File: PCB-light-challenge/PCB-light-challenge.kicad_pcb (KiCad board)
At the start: 2 copper layers, 1 part

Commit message: Footprints toegevoegd van alles
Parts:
- removed U-PICO2: ~, custom_footprint_pico:Pico_light challenge
- added 3V3: Screw_Terminal_01x02, Connector_PinHeader_2.54mm:PinHeader_1x02_P2.54mm_Horizontal, F.Cu at (74.2, 33.9)
- added 5V1: Screw_Terminal_01x02, Connector_PinHeader_2.54mm:PinHeader_1x02_P2.54mm_Horizontal, F.Cu at (75.3, 44.1)
- added Batterij1: Screw_Terminal_01x02, Connector_PinHeader_2.54mm:PinHeader_1x02_P2.54mm_Horizontal, F.Cu at (76.2, 53.7)
- added C1: 100n, Capacitor_SMD:C_0603_1608Metric, F.Cu at (211.5, 144.0)
- added C2: 100n, Capacitor_SMD:C_0603_1608Metric, F.Cu at (189.5, 140.0)
- added J2: Screw_Terminal_01x20, Connector_PinHeader_2.54mm:PinHeader_1x35_P2.54mm_Horizontal, F.Cu at (54.4, 23.3)
- added PIR_sens1: ~, PIRsens:PIR-SENS, F.Cu at (202.0, 126.0)
- added PS2: TMPW_5-105, TMPW_5-105:CONV_TMPW_5-105, F.Cu at (254.7, 135.7)
- added R1: 330, Resistor_SMD:R_0603_1608Metric, F.Cu at (206.1, 146.6)
- added R2: 2K7, Resistor_SMD:R_0603_1608Metric, F.Cu at (206.1, 149.1)
- added Shock_sens1: ~, Shocksens:Schock-sens, F.Cu at (179.7, 139.7)
- added U-PICO1: ~, Pico footprint:PICO, F.Cu at (215.1, 105.9)
- added U1: ~, BMS:bms, F.Cu at (167.7, 77.5)
- added U2: AP9101CK, Package_TO_SOT_SMD:SOT-23-5, F.Cu at (216.0, 136.1)
- added U3: SP8K32FRATB, MOSFET footprint:SOIC127P600X175-8N, F.Cu at (225.2, 135.6)
- added U4: ~, LDO:LDO- TO220FP, F.Cu at (198.5, 138.5)
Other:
- board outline added: 80.1 x 79.1 mm

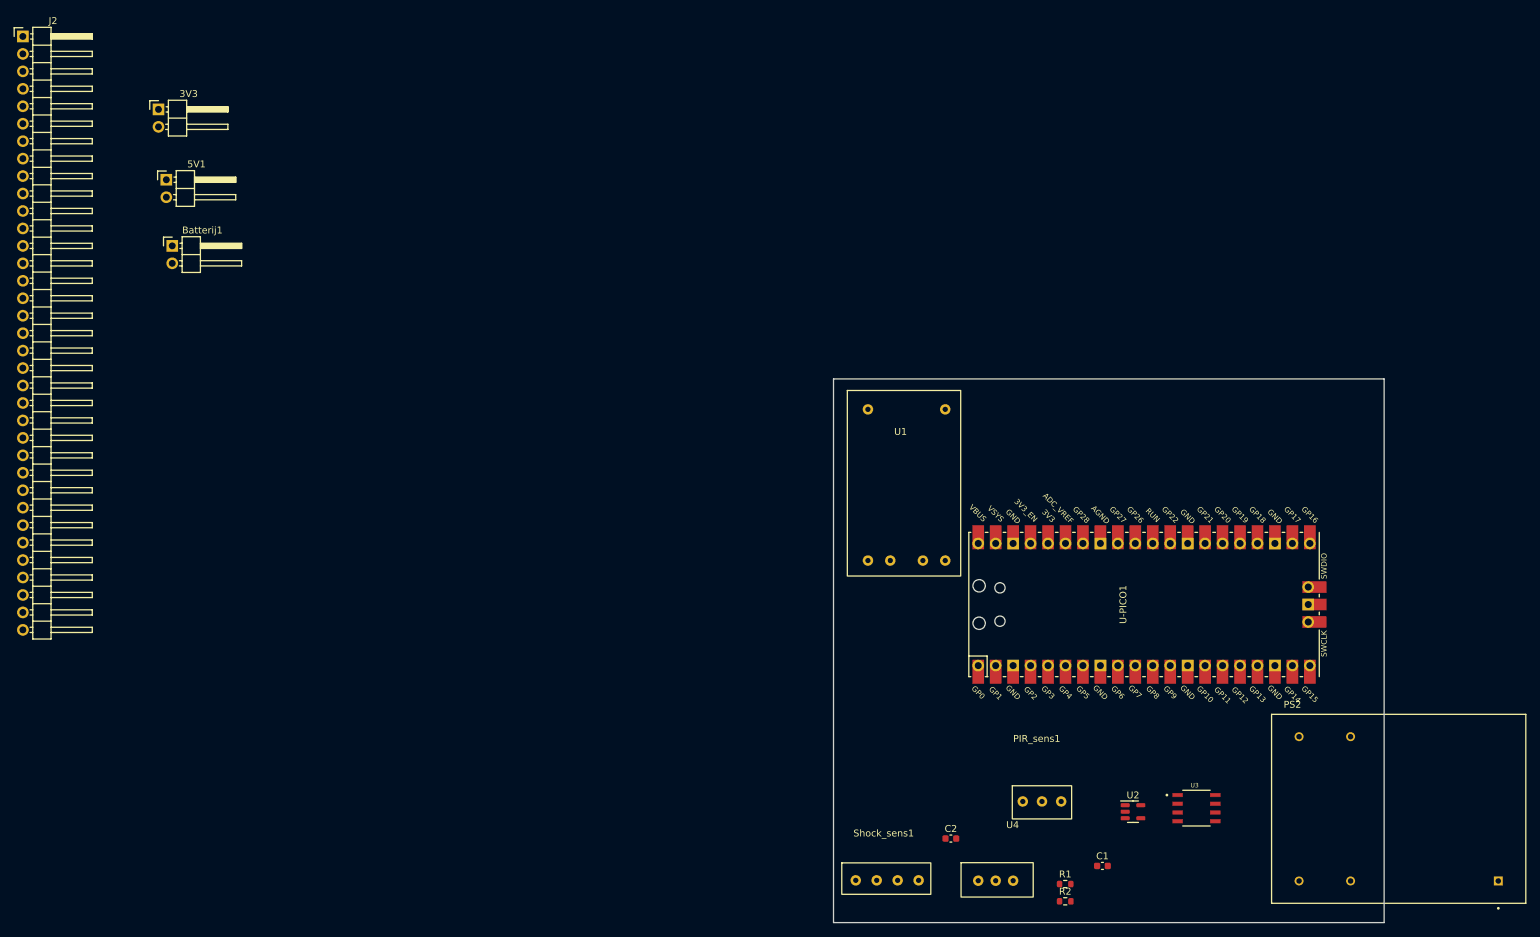
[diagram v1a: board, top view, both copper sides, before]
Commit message: Mainboard onderdelen gesorteerd
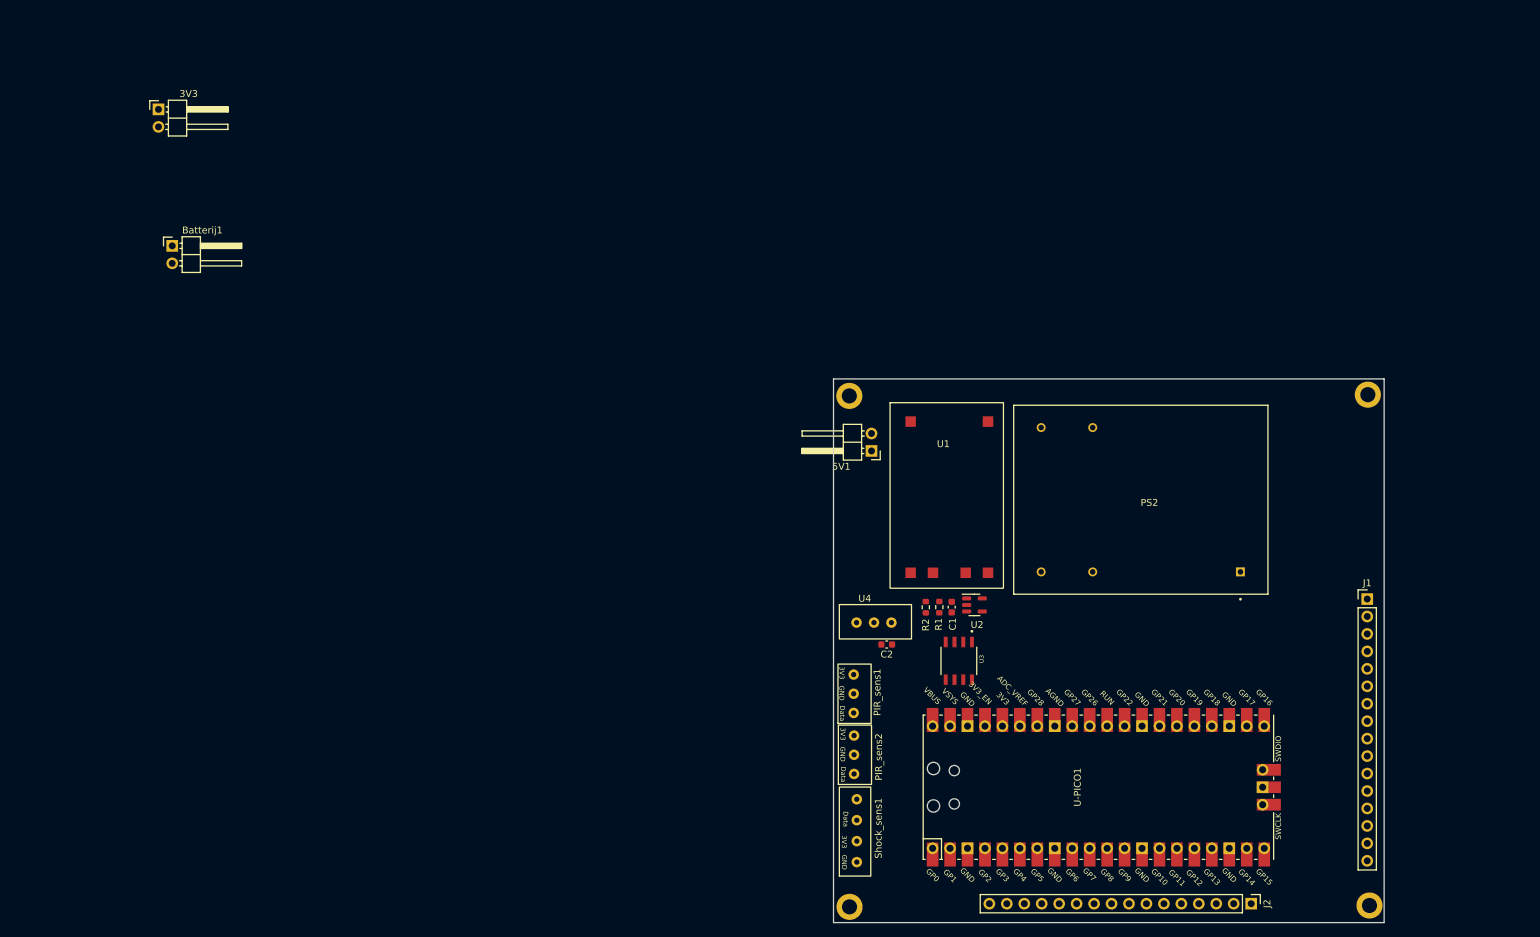
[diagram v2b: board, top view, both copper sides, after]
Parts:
- added H1: MountingHole_Pad, MountingHole:MountingHole_2.2mm_M2_DIN965_Pad, F.Cu at (174.7, 75.6)
- added H2: MountingHole_Pad, MountingHole:MountingHole_2.2mm_M2_DIN965_Pad, F.Cu at (250.4, 149.7)
- added H3: MountingHole_Pad, MountingHole:MountingHole_2.2mm_M2_DIN965_Pad, F.Cu at (250.2, 75.4)
- added H4: MountingHole_Pad, MountingHole:MountingHole_2.2mm_M2_DIN965_Pad, F.Cu at (174.7, 149.9)
- added J1: Conn_01x16_Socket, Connector_PinHeader_2.54mm:PinHeader_1x16_P2.54mm_Vertical, F.Cu at (250.1, 105.1)
- added PIR_sens2: ~, PIRsens:PIR-SENS, F.Cu at (166.8, 128.6)
- J2: value Screw_Terminal_01x20 -> Conn_01x16_Socket; footprint Connector_PinHeader_2.54mm:PinHeader_1x35_P2.54mm_Horizontal -> Connector_PinHeader_2.54mm:PinHeader_1x16_P2.54mm_Vertical
- moved J2 218.8 mm to (233.2, 149.5), turned to -90 degrees
- moved 5V1 110.0 mm to (177.9, 83.6), turned to 180 degrees
- moved PS2 58.6 mm to (217.1, 90.7)
- moved R2 47.4 mm to (185.8, 106.3), turned to -90 degrees
- moved R1 44.3 mm to (187.8, 106.3), turned to 90 degrees
- moved C1 43.6 mm to (189.6, 106.3), turned to -90 degrees
- moved U4 41.5 mm to (180.8, 100.9)
- moved U3 40.7 mm to (190.6, 114.1), turned to -90 degrees
- moved U2 37.9 mm to (192.9, 106.0)
- moved PIR_sens1 35.8 mm to (166.7, 119.7), turned to 90 degrees
- moved C2 29.7 mm to (180.1, 111.8), turned to 180 degrees
- moved U-PICO1 27.4 mm to (208.4, 132.5)
- moved Shock_sens1 10.3 mm to (169.4, 139.3), turned to 90 degrees
- moved U1 6.47 mm to (173.9, 79.3)
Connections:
- J2 pad 1: BAT- -> GP15
- J2 pad 10: GP28 -> GP6
- J2 pad 11: GP27 -> GP5
- J2 pad 12: GP26 -> GP4
- J2 pad 13: GP22 -> GP3
- J2 pad 14: GP21 -> GP2
- J2 pad 15: GP20 -> GP1
- J2 pad 16: GP19 -> GP0
- J2 pad 2: 3V3 -> GP14
- J2 pad 3: VBUS -> GP13
- J2 pad 4: RUN -> GP12
- J2 pad 5: ADC VREF -> GP11
- J2 pad 6: 3V3 OUT -> GP10
- J2 pad 7: 3V3 EN -> GP9
- J2 pad 8: SWDIO -> GP8
- J2 pad 9: SWCLK -> GP7
- U-PICO1 pad 1: (no net) -> GP0
- U-PICO1 pad 10: (no net) -> GP7
- U-PICO1 pad 11: (no net) -> GP8
- U-PICO1 pad 12: (no net) -> GP9
- U-PICO1 pad 13: (no net) -> BAT-
- U-PICO1 pad 14: (no net) -> GP10
- U-PICO1 pad 15: (no net) -> GP11
- U-PICO1 pad 16: (no net) -> GP12
- U-PICO1 pad 17: (no net) -> GP13
- U-PICO1 pad 18: (no net) -> BAT-
- U-PICO1 pad 19: (no net) -> GP14
- U-PICO1 pad 2: (no net) -> GP1
- U-PICO1 pad 20: (no net) -> GP15
- U-PICO1 pad 21: (no net) -> GP16
- U-PICO1 pad 22: (no net) -> GP17
- U-PICO1 pad 23: (no net) -> BAT-
- U-PICO1 pad 24: (no net) -> GP18
- U-PICO1 pad 25: (no net) -> GP19
- U-PICO1 pad 26: (no net) -> GP20
- U-PICO1 pad 27: (no net) -> GP21
- U-PICO1 pad 28: (no net) -> BAT-
- U-PICO1 pad 29: (no net) -> GP22
- U-PICO1 pad 3: (no net) -> BAT-
- U-PICO1 pad 30: (no net) -> RUN
- U-PICO1 pad 31: (no net) -> GP26
- U-PICO1 pad 32: (no net) -> GP27
- U-PICO1 pad 33: (no net) -> BAT-
- U-PICO1 pad 34: (no net) -> GP28
- U-PICO1 pad 35: (no net) -> ADC VREF
- U-PICO1 pad 36: (no net) -> 3V3 OUT
- U-PICO1 pad 37: (no net) -> 3V3 EN
- U-PICO1 pad 38: (no net) -> BAT-
- U-PICO1 pad 39: (no net) -> 3V3
- U-PICO1 pad 4: (no net) -> GP2
- U-PICO1 pad 40: (no net) -> VBUS
- U-PICO1 pad 5: (no net) -> GP3
- U-PICO1 pad 6: (no net) -> GP4
- U-PICO1 pad 7: (no net) -> GP5
- U-PICO1 pad 8: (no net) -> BAT-
- U-PICO1 pad 9: (no net) -> GP6
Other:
- board text added: "3V3"
- board text added: "Data"
- board text added: "GND"

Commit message: main board aangepast en ground toegevoegd
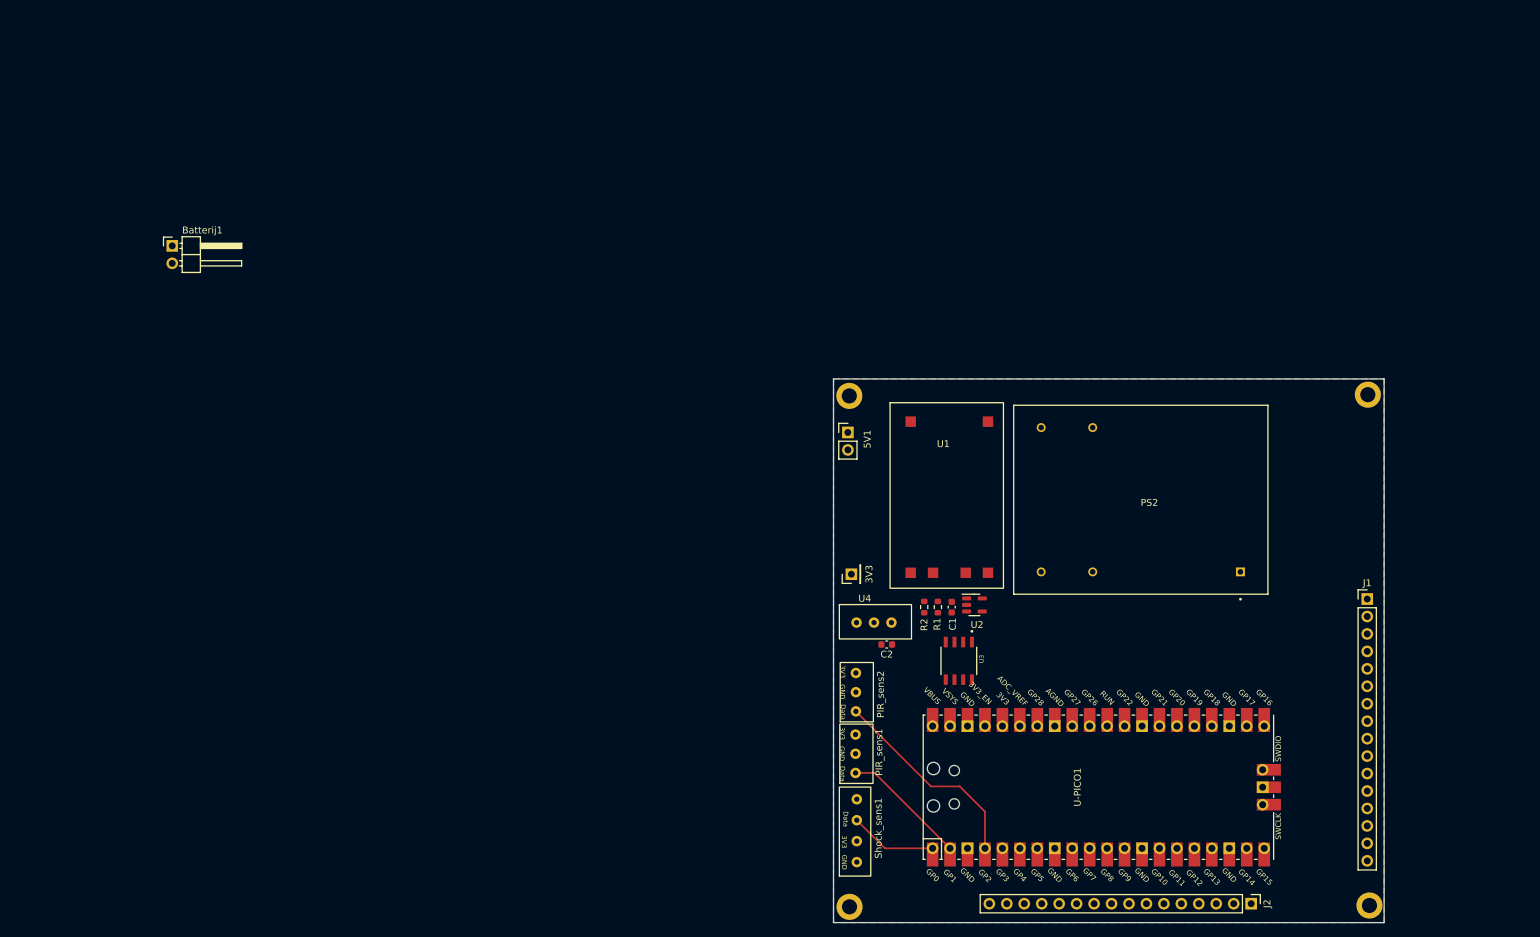
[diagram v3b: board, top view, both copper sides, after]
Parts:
- 3V3: value Screw_Terminal_01x02 -> Conn_01x01_Socket; footprint Connector_PinHeader_2.54mm:PinHeader_1x02_P2.54mm_Horizontal -> Connector_PinHeader_2.54mm:PinHeader_1x01_P2.54mm_Vertical
- 5V1: value Screw_Terminal_01x02 -> Conn_01x02_Socket; footprint Connector_PinHeader_2.54mm:PinHeader_1x02_P2.54mm_Horizontal -> Connector_PinHeader_2.54mm:PinHeader_1x02_P2.54mm_Vertical
- moved 3V3 121.4 mm to (175.0, 101.5), turned to 90 degrees
- moved PIR_sens2 9.11 mm to (167.0, 119.4)
- moved PIR_sens1 8.73 mm to (167.0, 128.4)
- moved 5V1 4.37 mm to (174.5, 80.9), turned to 0 degrees
- moved R2 0.23 mm to (185.6, 106.3)
- moved R1 0.21 mm to (187.6, 106.3)
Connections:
- net /Battery_charger/5Vin renamed Net-(PS2-+VOUT)
- net /Battery_charger/GND1 renamed Net-(PS2--VOUT)
- 3V3 pad 1: BAT- -> 3V3
- 5V1 pad 1: BAT- -> GND
- Batterij1 pad 1: BAT- -> GND
- C1 pad 2: BAT- -> GND
- C2 pad 2: BAT- -> GND
- H1 pad 1: BAT- -> GND
- H2 pad 1: BAT- -> GND
- H3 pad 1: BAT- -> GND
- H4 pad 1: BAT- -> GND
- PIR_sens1 pad 2: BAT- -> GND
- PIR_sens1 pad 3: OUT DATA -> GP1
- PIR_sens2 pad 2: BAT- -> GND
- PIR_sens2 pad 3: OUT DATA2 -> GP2
- Shock_sens1 pad 2: Digital Out Shocksens -> GP0
- Shock_sens1 pad 4: BAT- -> GND
- U-PICO1 pad 13: BAT- -> GND
- U-PICO1 pad 18: BAT- -> GND
- U-PICO1 pad 23: BAT- -> GND
- U-PICO1 pad 28: BAT- -> GND
- U-PICO1 pad 3: BAT- -> GND
- U-PICO1 pad 33: BAT- -> GND
- U-PICO1 pad 38: BAT- -> GND
- U-PICO1 pad 8: BAT- -> GND
- U1 pad 4: BAT- -> GND
- U2 pad 3: BAT- -> GND
- U3 pad 3: BAT- -> GND
- U4 pad 2: BAT- -> GND
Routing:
- net GP2: track 0.00 -> 30.2 mm
- net GP1: track 0.00 -> 18.3 mm
- net GP0: track 0.00 -> 12.7 mm
- added copper zone on B.Cu, net GND
- added copper zone on In1.Cu, net GND
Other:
- copper layers 2 -> 4
